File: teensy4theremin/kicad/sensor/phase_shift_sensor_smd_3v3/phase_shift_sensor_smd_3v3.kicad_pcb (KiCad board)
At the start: 2 copper layers, 70.5 x 19.8 mm, 32 parts, among them J1 SENSOR, J2 INDUCTOR_IN, J3 INDUCTOR_OUT, J4 ANTENNA, U1 LVC2G14, U2 4220CZ6, U3 MCP1700-3302E, U4 LVC2G04, U5 4220CZ6, U6 MCP1700-3302E

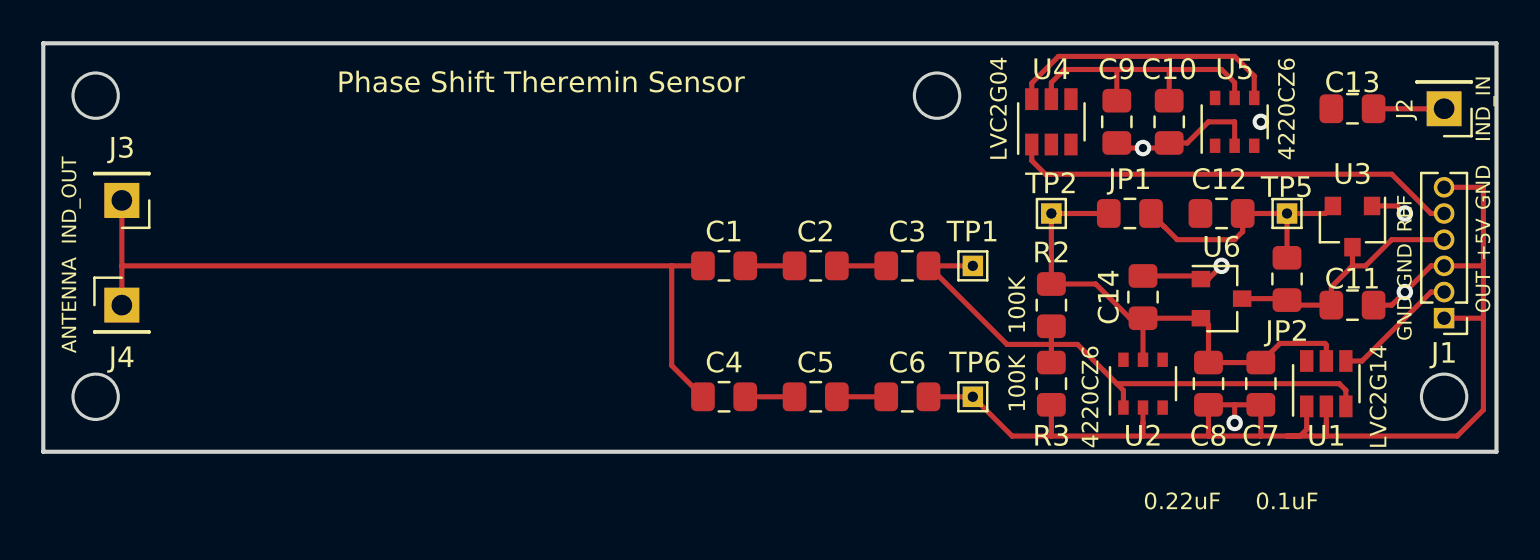
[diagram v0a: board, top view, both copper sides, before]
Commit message: phase shift sensor - new
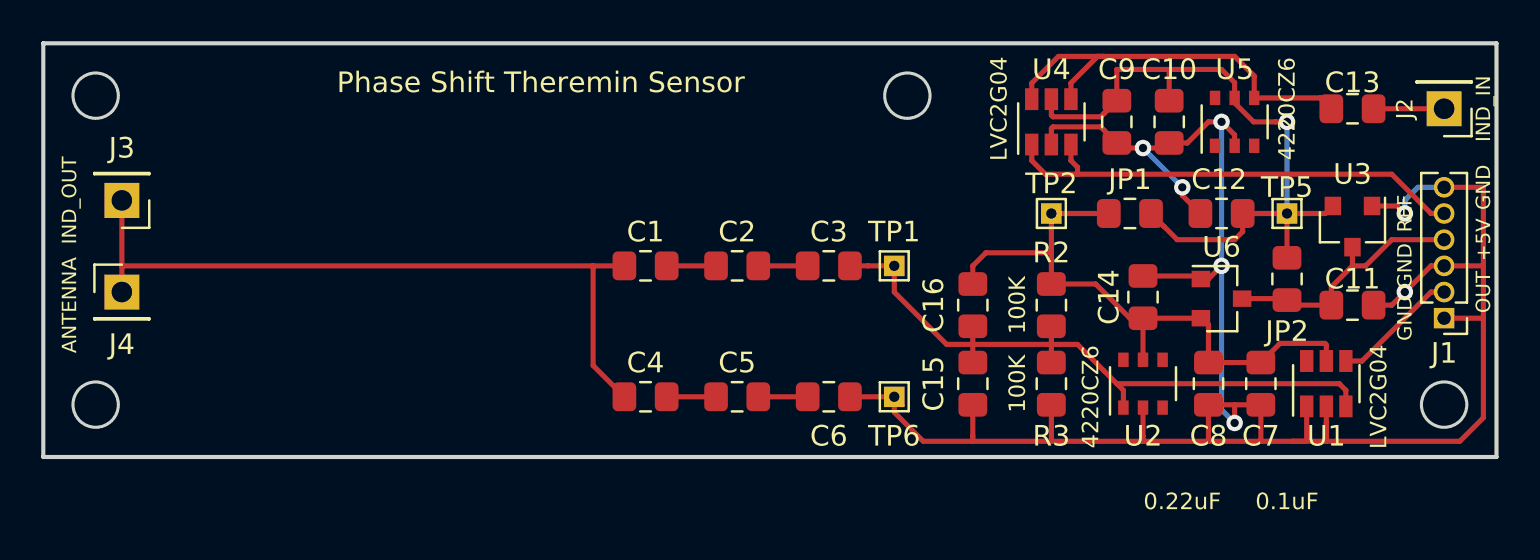
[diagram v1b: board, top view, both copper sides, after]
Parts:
- added C15: 3.3pF, Capacitor_SMD:C_0805_2012Metric_Pad1.15x1.40mm_HandSolder, F.Cu at (126.4, 110.5)
- added C16: 3.3pF, Capacitor_SMD:C_0805_2012Metric_Pad1.15x1.40mm_HandSolder, F.Cu at (126.4, 106.7)
- U1: value LVC2G14 -> LVC2G04
- moved C1 3.81 mm to (110.5, 104.8)
- moved C2 3.81 mm to (114.9, 104.8)
- moved C3 3.81 mm to (119.4, 104.8)
- moved C4 3.81 mm to (110.5, 111.1)
- moved C5 3.81 mm to (114.9, 111.1)
- moved C6 3.81 mm to (119.4, 111.1)
- moved TP1 3.81 mm to (122.6, 104.8)
- moved TP6 3.81 mm to (122.6, 111.1)
- moved J4 0.64 mm to (85.1, 106.0)
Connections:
- net VCC renamed Net-(C14-Pad1)
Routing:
- net GND: track 76.0 -> 110.3 mm, vias 6 -> 7
- net +3V3: track 27.1 -> 34.8 mm, vias 0 -> 1
- net Net-(C13-Pad2): track 13.6 -> 20.4 mm
- net Net-(C14-Pad1): track 25.4 -> 30.4 mm
- net Net-(C15-Pad1): track 28.7 -> 32.9 mm
- net Net-(C1-Pad1): track 40.2 -> 36.4 mm
- net /REF_CLK: track 21.8 -> 23.4 mm
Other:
- board size 70.5 x 19.8 mm -> 70.5 x 20.1 mm
